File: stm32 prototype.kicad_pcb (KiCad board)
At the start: 4 copper layers, 22.9 x 66 mm, 41 parts, among them J1 Conn_01x25, J10 Conn_01x03, J2 Conn_02x05_Odd_Even, J8 Conn_01x25, J9 Conn_01x03, Q1 Q_NMOS_GSD, SW1 SW_Push, SW2 SW_Push, U1 STM32F405RGTx, U7 TPS62203DBVR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

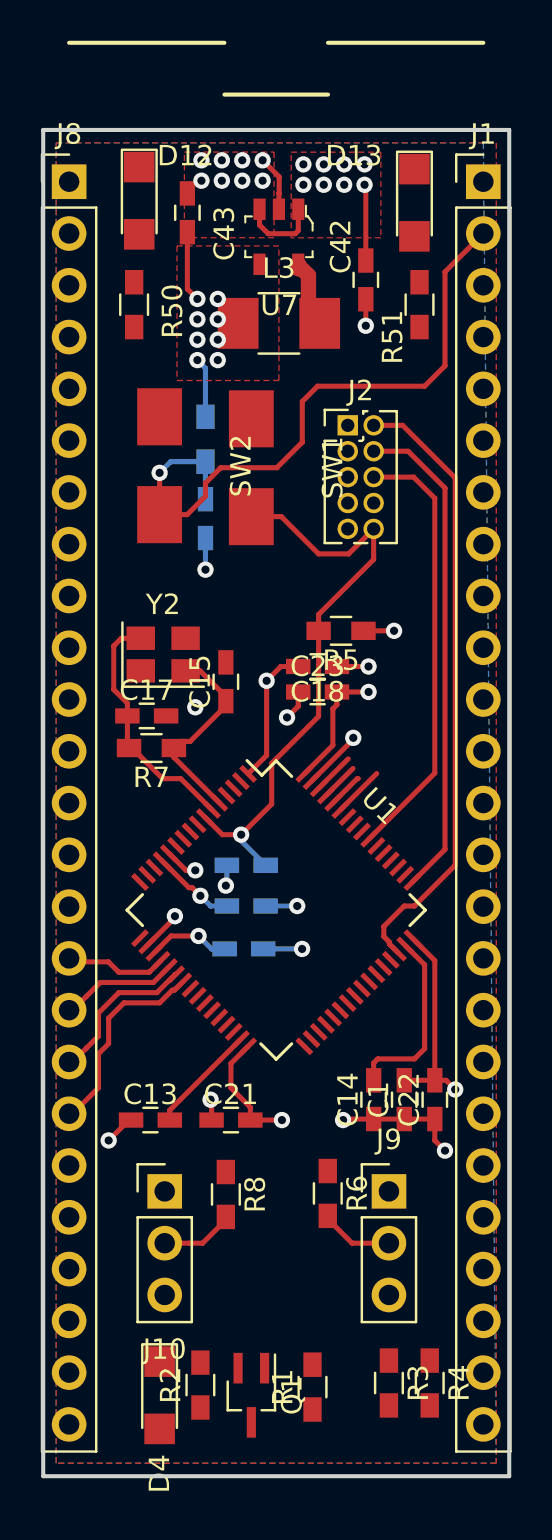
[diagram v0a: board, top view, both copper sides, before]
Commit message: finished layout, need to do final review before ordering PCB
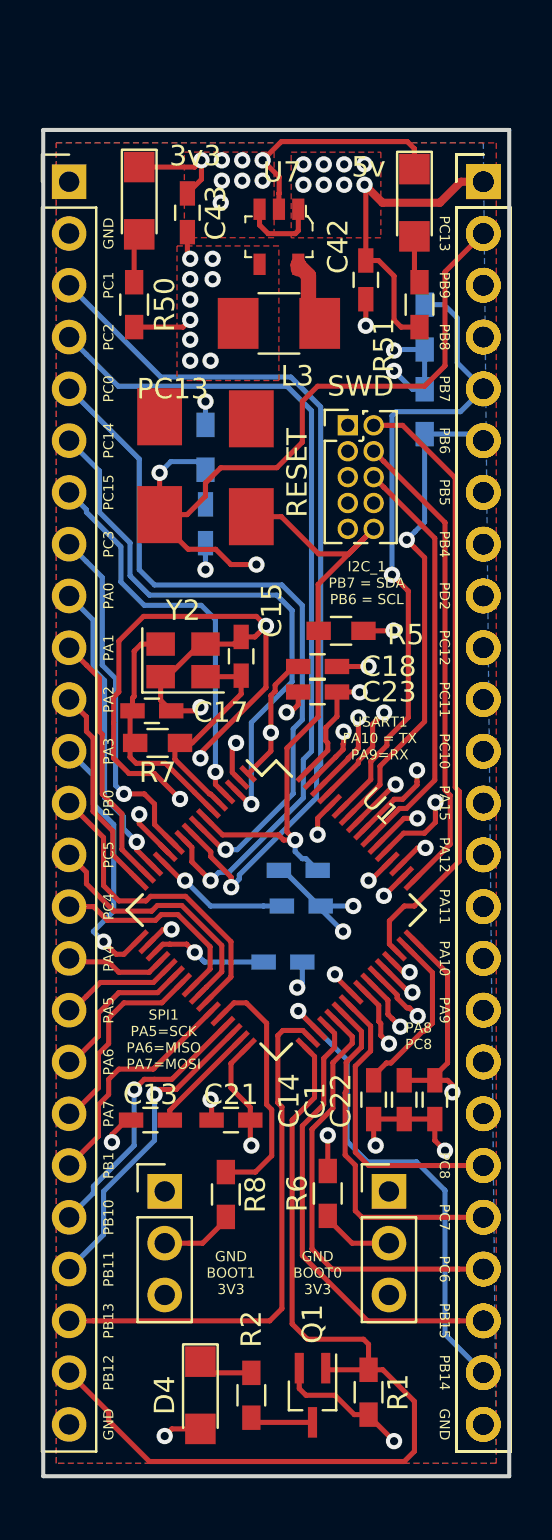
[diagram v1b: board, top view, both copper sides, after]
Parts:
- added J1 (x2): Conn_01x25, Pin_Headers:Pin_Header_Straight_1x25_Pitch2.54mm, F.Cu at (182.9, 45.7)
- R3, R4: moved to B.Cu
- moved R4 51.8 mm to (180.0, 52.9), turned to 90 degrees
- moved R3 47.7 mm to (180.0, 57.0)
- moved Q1 3.00 mm to (174.5, 105.2)
- moved R1 2.76 mm to (177.2, 105.1), turned to 270 degrees
- moved C24 2.70 mm to (173.9, 81.2)
- moved C12 2.56 mm to (173.8, 79.5)
- moved R2 2.55 mm to (171.5, 105.2), turned to 270 degrees
- moved C19 2.02 mm to (173.1, 84.0)
- moved D4 2.00 mm to (169.0, 105.2)
- moved C15 1.46 mm to (171.0, 69.0)
- moved Y2 1.02 mm to (168.2, 69.2)
- moved R32 0.40 mm to (169.2, 58.8)
- moved R7 0.39 mm to (166.9, 73.2)
- moved C17 0.35 mm to (166.6, 71.7)
- moved C20 0.25 mm to (169.2, 62.5)
- renumbered D12 to 3v3, D13 to 5v, SW2 to PC13, SW1 to RESET, J2 to SWD
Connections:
- C20 pad 2: PA0 -> PC13
- J1 pad 10: PA8_MCO -> PC12
- J1 pad 11: PA9_ST_RXD -> PC11
- J1 pad 12: PA10_ST_TXD -> PC10
- J1 pad 13: PA11_ST_RTS -> PA15
- J1 pad 15: PA15 -> PA11_ST_RTS
- J1 pad 16: PB0 -> PA10_ST_TXD
- J1 pad 17: PB1 -> PA9_ST_RXD
- J1 pad 18: (no net) -> PA8_MCO
- J1 pad 19: PB4 -> PC9
- J1 pad 2: PA0 -> PC13
- J1 pad 20: PB5_I2C1_SMBA -> PC8
- J1 pad 21: PB6_I2C1_SCL -> PC7
- J1 pad 22: PB7_I2C1_SDA -> PC6
- J1 pad 23: PB8 -> PB15
- J1 pad 24: PB9 -> PB14
- J1 pad 3: PA1 -> PB9
- J1 pad 4: PA2 -> PB8
- J1 pad 5: PA3 -> PB7_I2C1_SDA
- J1 pad 6: PC11 -> PB6_I2C1_SCL
- J1 pad 7: PC12 -> PB5_I2C1_SMBA
- J1 pad 8: PC13 -> PB4
- J1 pad 9: PC14 -> PD2
- J8 pad 10: PC7 -> PA1
- J8 pad 11: PC8 -> PA2
- J8 pad 12: PC9 -> PA3
- J8 pad 13: PC10 -> PB0
- J8 pad 14: PC15_STATUS -> PC5
- J8 pad 15: PB10 -> PC4
- J8 pad 2: PD2 -> GND
- J8 pad 20: PB11 -> PB1
- J8 pad 21: PB12 -> PB10
- J8 pad 22: PB13 -> PB11
- J8 pad 23: PB14 -> PB13
- J8 pad 24: PB15 -> PB12
- J8 pad 3: PC0 -> PC1
- J8 pad 4: PC1 -> PC2
- J8 pad 5: PC2 -> PC0
- J8 pad 6: PC3 -> PC14
- J8 pad 7: PC4 -> PC15
- J8 pad 8: PC5 -> PC3
- J8 pad 9: PC6 -> PA0
- PC13 pad 1: PA0 -> PC13
- Q1 pad 1: PC15_STATUS -> PB12
- R1 pad 1: PC15_STATUS -> PB12
- R32 pad 2: PA0 -> PC13
- U1 pad 4: PC15_STATUS -> PC15
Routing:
- net GND: track 28.8 -> 88.7 mm, vias 23 -> 27
- net PC13: track 0.00 -> 50.9 mm, vias 0 -> 3
- net PB12: track 0.00 -> 46.5 mm
- net PC1: track 0.00 -> 43.8 mm, vias 0 -> 1
- net PC2: track 0.00 -> 41.4 mm, vias 0 -> 1
- net PC0: track 0.00 -> 34.8 mm, vias 0 -> 1
- net PB7_I2C1_SDA: track 2.53 -> 32.0 mm, vias 0 -> 1
- net PC14: track 0.00 -> 28.0 mm, vias 0 -> 1
- net PB9: track 2.04 -> 28.3 mm, vias 0 -> 1
- net PB13: track 0.00 -> 26.1 mm
- net PB14: track 0.00 -> 24.3 mm, vias 0 -> 1
- net PB6_I2C1_SCL: track 0.00 -> 24.1 mm, vias 0 -> 1
- net PB8: track 1.88 -> 25.7 mm, vias 0 -> 1
- net PB15: track 0.00 -> 22.4 mm
- net PC6: track 0.00 -> 21.4 mm
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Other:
- board text added: "GND"
- board text added: "GND BOOT0 3V3"
- board text added: "GND BOOT1 3V3"
- board text added: "I2C_1 PB7 = SDA PB6 = SCL"
- board text added: "PA0"
- board text added: "PA1"
- board text added: "PA10"
- board text added: "PA11"
- board text added: "PA12"
- board text added: "PA15"
- board text added: "PA2"
- board text added: "PA3"
- board text added: "PA4"
- board text added: "PA5"
- board text added: "PA6"
- board text added: "PA7"
- board text added: "PA8 PC8"
- board text added: "PA9"
- board text added: "PB0"
- board text added: "PB1"
- board text added: "PB10"
- board text added: "PB11"
- board text added: "PB12"
- board text added: "PB13"
- board text added: "PB14"
- board text added: "PB15"
- board text added: "PB4"
- board text added: "PB5"
- board text added: "PB6"
- board text added: "PB7"
- board text added: "PB8"
- board text added: "PB9"
- board text added: "PC0"
- board text added: "PC1"
- board text added: "PC10"
- board text added: "PC11"
- board text added: "PC12"
- board text added: "PC13"
- board text added: "PC14"
- board text added: "PC15"
- board text added: "PC2"
- board text added: "PC3"
- board text added: "PC4"
- board text added: "PC5"
- board text added: "PC6"
- board text added: "PC7"
- board text added: "PC8"
- board text added: "PD2"
- board text added: "SPI1 PA5=SCK PA6=MISO PA7=MOSI"
- board text added: "USART1 PA10 = TX PA9=RX"

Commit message: Ordered PCB from OSHPark
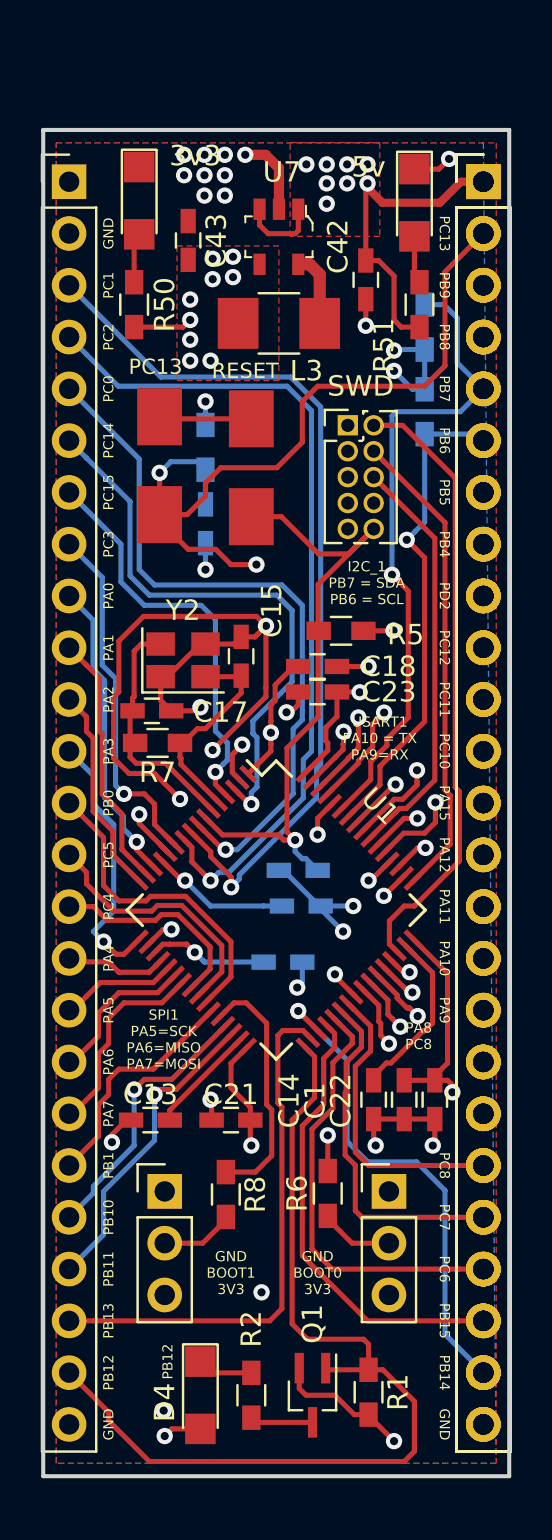
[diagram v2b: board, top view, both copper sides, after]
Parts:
- moved C43 1.36 mm to (168.4, 48.6)
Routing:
- net GND: track 88.7 -> 80.6 mm, vias 27 -> 31
- net PC13: track 50.9 -> 49.5 mm
- net +3V3: track 55.5 -> 54.2 mm
- net Net-(C15-Pad1): track 11.0 -> 10.4 mm
